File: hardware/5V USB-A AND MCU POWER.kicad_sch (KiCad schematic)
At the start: 34 parts, among them U19 NCP177BMX330TCG, U2 NCP177BMX330TCG, U3 NCP177BMX330TCG, U4 LMR14050-Q1, U5 NCP177AMX120TCG, U6 NCP177AMX120TCG

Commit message: messing arround with pcb to finalise
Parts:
- added TP12: TestPoint, TestPoint:TestPoint_Pad_D1.5mm, symbol Connector:TestPoint
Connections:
- net +5V: now also TP12.1
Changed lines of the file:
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@@
   (junction (at 67.31 124.46) (diameter 0) (color 0 0 0 0)
   )
+  (junction (at 151.13 68.58) (diameter 0) (color 0 0 0 0)
+  )
   (junction (at 33.02 160.02) (diameter 0) (color 0 0 0 0)
   )
@@
     (stroke (width 0) (type default))
   )
+  (wire (pts (xy 151.13 68.58) (xy 153.67 68.58))
+    (stroke (width 0) (type default))
+  )
   (wire (pts (xy 144.78 124.46) (xy 149.86 124.46))
     (stroke (width 0) (type default))
@@
     (stroke (width 0) (type default))
   )
-  (wire (pts (xy 148.59 68.58) (xy 153.67 68.58))
+  (wire (pts (xy 148.59 68.58) (xy 151.13 68.58))
     (stroke (width 0) (type default))
   )
@@
         )
       )
+    )
+  )
+  (symbol (lib_id "Connector:TestPoint") (at 151.13 68.58 0) (unit 1)
+    (in_bom yes) (on_board yes) (dnp no) (fields_autoplaced)
+    (property "Reference" "TP12" (at 152.527 64.6343 0)
+      (effects (font (size 1.27 1.27)) (justify left))
+    )
+    (property "Value" "TestPoint" (at 152.527 66.5553 0)
+      (effects (font (size 1.27 1.27)) (justify left))
+    )
+    (property "Footprint" "TestPoint:TestPoint_Pad_D1.5mm" (at 156.21 68.58 0)
+      (effects (font (size 1.27 1.27)) hide)
+    )
+    (property "Datasheet" "~" (at 156.21 68.58 0)
+      (effects (font (size 1.27 1.27)) hide)
+    )
+    (pin "1")
+    (instances
+      (project "usbc-car-module"
+        (path "/fae025e9-99c5-40c1-af6f-99dc1edbfa43/babd34fb-a18a-4bce-9735-4ab8ec7cd7ca"
+          (reference "TP12") (unit 1)
+        )
+      )

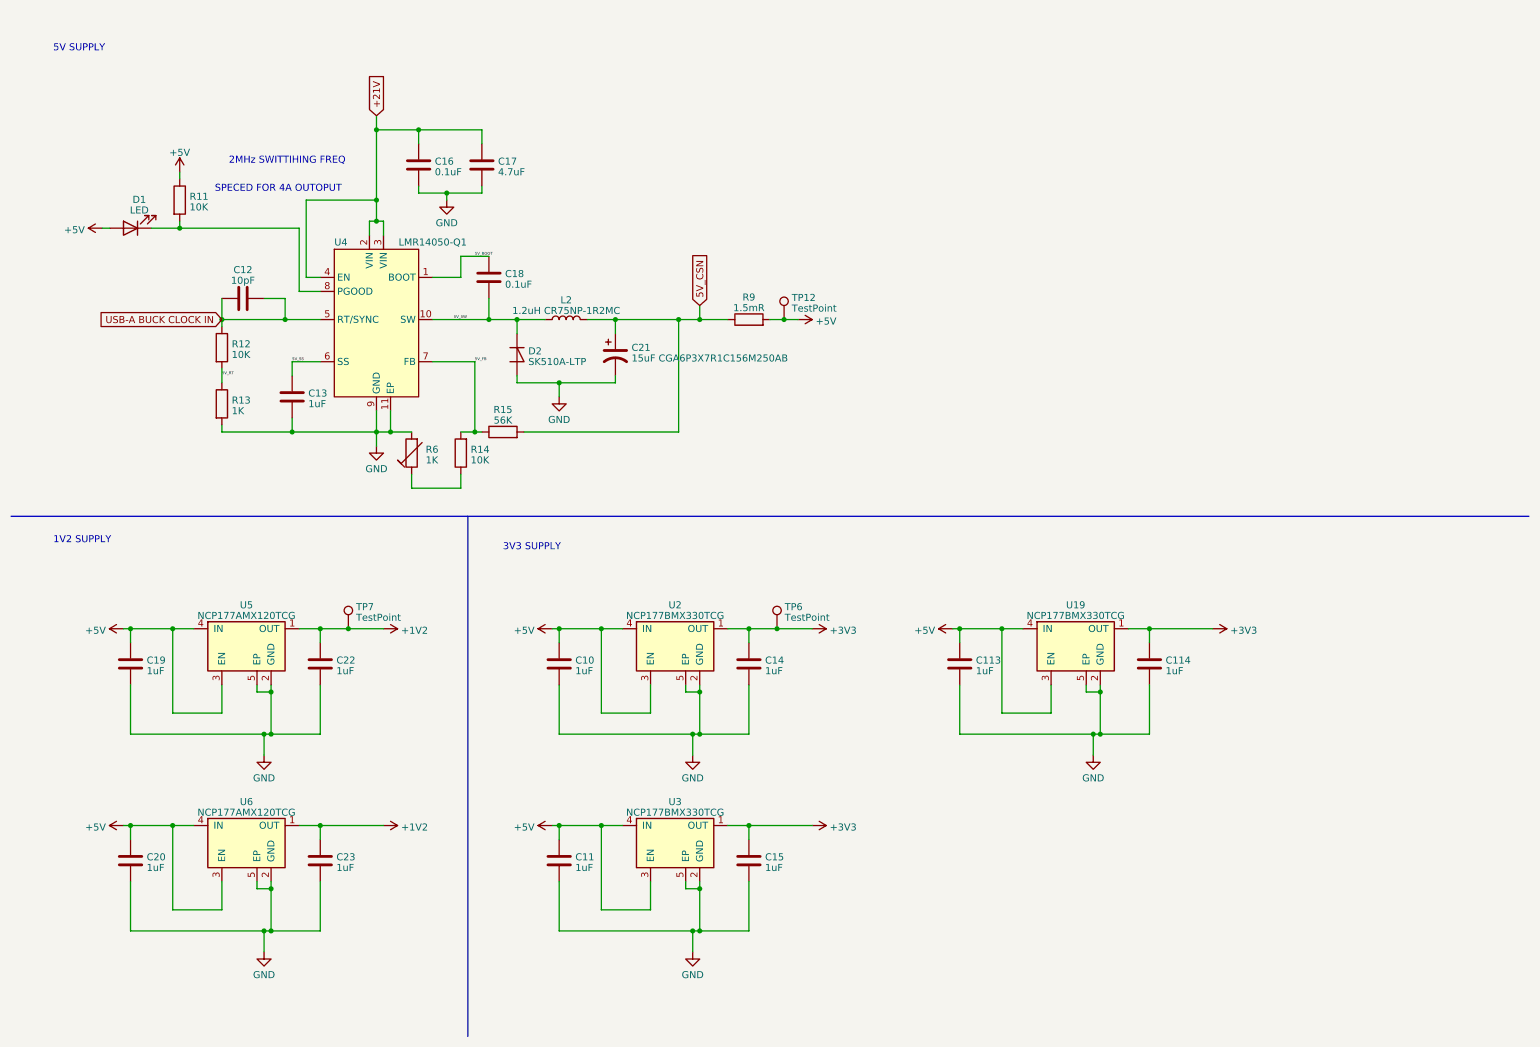
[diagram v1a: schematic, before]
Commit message: fixed DP issues and finneshed overall routeing
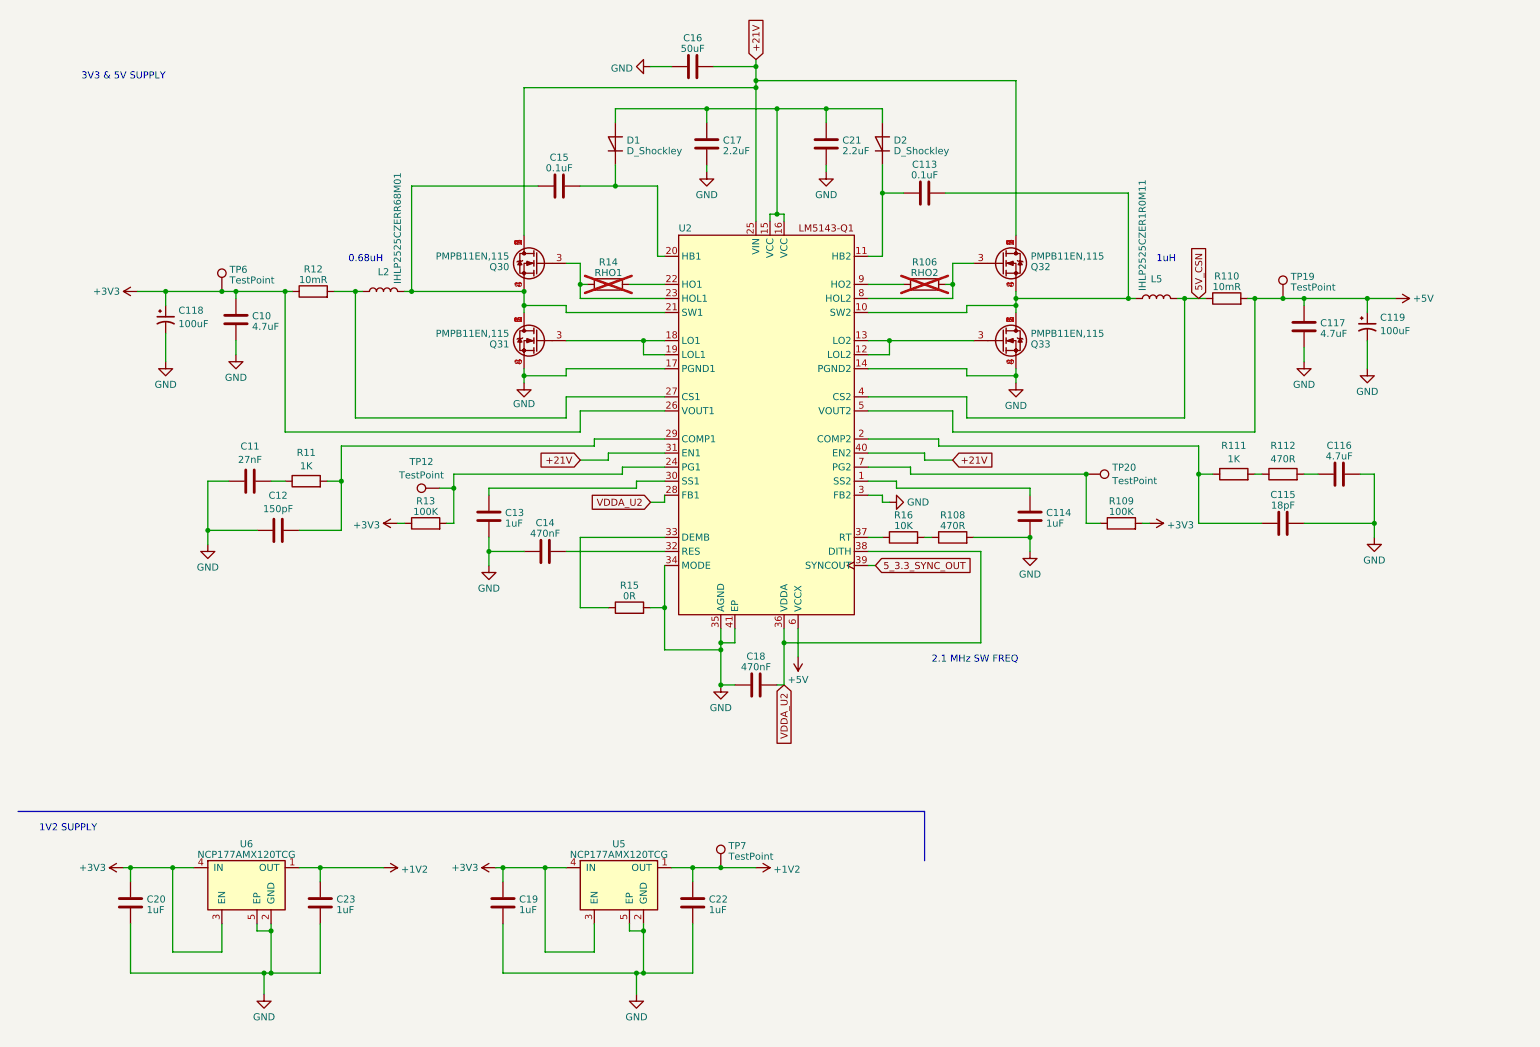
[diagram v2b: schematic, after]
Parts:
- removed C21: 15uF CGA6P3X7R1C156M250AB, Capacitor_SMD:C_1210_3225Metric, symbol Device:C_Polarized_US
- removed D1: LED, Diode_SMD:D_0603_1608Metric, symbol Device:LED
- removed R6: 1K, PCM_Potentiometer_SMD_AKL:Potentiometer_Bourns_TC33X_Vertical, symbol Device:R_Trim
- removed R9: 1.5mR, Resistor_SMD:R_2512_6332Metric, symbol Device:R
- removed U19, U2, U3: NCP177BMX330TCG, CARTHING:VREG_NCP170AMX300TCG, symbol CARTHING:NCP177BMX330TCG-Regulator_Linear
- removed U4: LMR14050-Q1, CARTHING:LMR14050, symbol EXTRA:LMR14050-Q1
- added C115: 18pF, Capacitor_SMD:C_0603_1608Metric, symbol Device:C
- added C116, C117: 4.7uF, Capacitor_SMD:C_0603_1608Metric, symbol Device:C
- added C118, C119: 100uF, Capacitor_SMD:CP_Elec_6.3x7.7, symbol Device:C_Polarized_Small_US
- added C21: 2.2uF, Capacitor_SMD:C_0603_1608Metric, symbol Device:C
- added D1: D_Shockley, Diode_SMD:D_SMA, symbol Device:D_Shockley
- added L5: IHLP2525CZER1R0M11, CARTHING:IND25X25CZ, symbol Device:L
- added Q30, Q31, Q32, Q33: PMPB11EN,115, CARTHING:TRANS_PMPB11EN_115, symbol Device:Q_NMOS_GDS
- added R106: RHO2, Resistor_SMD:R_0603_1608Metric, symbol Device:R
- added R108, R112: 470R, Resistor_SMD:R_0603_1608Metric, symbol Device:R
- added R109: 100K, Resistor_SMD:R_0603_1608Metric, symbol Device:R
- added R110: 10mR, Resistor_SMD:R_1206_3216Metric, symbol Device:R
- added R111: 1K, Resistor_SMD:R_0603_1608Metric, symbol Device:R
- added R16: 10K, Resistor_SMD:R_0603_1608Metric, symbol Device:R
- added TP19: TestPoint, TestPoint:TestPoint_Pad_D1.5mm, symbol Connector:TestPoint
- added TP20: TestPoint, TestPoint:TestPoint_Pad_D1.0mm, symbol Connector:TestPoint
- added U2: ~, CARTHING:LM5143, symbol CARTHING:LM5143-Q1
- C10: value 1uF -> 4.7uF
- C11: value 1uF -> 27nF
- C113, C15: value 1uF -> 0.1uF
- C12: value 10pF -> 150pF
- C14: value 1uF -> 470nF; footprint Capacitor_SMD:C_0603_1608Metric -> Capacitor_SMD:C_0805_2012Metric
- C16: value 0.1uF -> 50uF
- C17: value 4.7uF -> 2.2uF
- C18: value 0.1uF -> 470nF; footprint Capacitor_SMD:C_0603_1608Metric -> Capacitor_SMD:C_0805_2012Metric
- D2: value SK510A-LTP -> D_Shockley
- L2: value 1.2uH CR75NP-1R2MC -> IHLP2525CZERR68M01
- R11: value 10K -> 1K
- R12: value 10K -> 10mR; footprint Resistor_SMD:R_0603_1608Metric -> Resistor_SMD:R_1206_3216Metric
- R13: value 1K -> 100K
- R14: value 10K -> RHO1; now not fitted
- R15: value 56K -> 0R
- TP12: footprint TestPoint:TestPoint_Pad_D1.5mm -> TestPoint:TestPoint_Pad_D1.0mm
- TP6: footprint TestPoint:TestPoint_Pad_D1.0mm -> TestPoint:TestPoint_Pad_D1.5mm
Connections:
- net 5V_BOOT is gone; now on net GND: C18.1
- net 5V_SS is gone; now on net GND: C13.1
- net +21V: now also C16.2, Q30.1 (D), Q30.2 (D), Q30.5 (D), Q30.6 (D), Q30.7 (D), Q32.1 (D), Q32.2 (D), Q32.5 (D), Q32.6 (D), Q32.7 (D), U2.25 (VIN), U2.31 (EN1), U2.40 (EN2); no longer C16.1, C17.1
- net +3V3: now also C10.1, C19.1, C20.1, R12.1, R13.1, U5.3 (EN), U5.4 (IN), U6.3 (EN), U6.4 (IN), C118.1, R109.2, U2.26 (VOUT1); no longer C114.1, C14.1, C15.1
- net +5V: now also C117.1, C119.1, R110.2, TP19.1, U2.5 (VOUT2), U2.6 (VCCX); no longer C10.1, C11.1, C113.1, C19.1, C20.1, R11.1, TP12.1, U5.3 (EN), U5.4 (IN), U6.3 (EN), U6.4 (IN)
- net 5V_CSN: now also L5.2, R110.1, U2.4 (CS2); no longer L2.2, R15.2
- net GND: now also C11.1, C114.1, C12.1, C14.1, C16.1, R15.2, C115.2, C116.2, C117.2, C118.2, C119.2, C21.2, Q31.4 (S), Q31.8 (S), Q33.4 (S), Q33.8 (S), R108.2, U2.14 (PGND2), U2.17 (PGND1), U2.3 (FB2), U2.34 (MODE), U2.35 (AGND), U2.41 (EP); no longer C11.2, C113.2, C114.2, C13.2, C14.2, C15.2, C16.2, D2.2 (A), R13.2
- net at R11.2: now also C12.2, U2.29 (COMP1)
- net at R14.1: now also Q30.3 (G), U2.23 (HOL1)
- net 5V_FB: no longer names the net of R14.2
- net 5V_FB: now also U2.22 (HO1); no longer R15.1
- net 5V_RT: no longer names the net of R12.2
- net 5V_RT: now also L2.1, U2.27 (CS1); no longer R13.1
- removed net 5V_SW: C18.2, D2.1 (K), L2.1
- removed net USB-A BUCK CLOCK IN: C12.1, C12.2, R12.1
- new net: C114.2, U2.1 (SS2)
- new net: C113.2, L5.1, Q32.4 (S), Q32.8 (S), Q33.1 (D), Q33.2 (D), Q33.5 (D), Q33.6 (D), Q33.7 (D), U2.10 (SW2)
- new net: C113.1, D2.1 (K), U2.11 (HB2)
- new net: Q33.3 (G), U2.12 (LOL2), U2.13 (LO2)
- new net: C17.1, C21.1, D1.2 (A), D2.2 (A), U2.15 (VCC), U2.16 (VCC)
- new net: Q31.3 (G), U2.18 (LO1), U2.19 (LOL1)
- new net: C115.1, R111.1, U2.2 (COMP2)
- new net: C15.2, D1.1 (K), U2.20 (HB1)
- new net: C15.1, L2.2, Q30.4 (S), Q30.8 (S), Q31.1 (D), Q31.2 (D), Q31.5 (D), Q31.6 (D), Q31.7 (D), U2.21 (SW1)
- new net: R13.2, TP12.1, U2.24 (PG1)
- new net: C13.2, U2.30 (SS1)
- new net: C14.2, U2.32 (RES)
- new net: R15.1, U2.33 (DEMB)
- new net: R16.1, U2.37 (RT)
- new net: R109.1, TP20.1, U2.7 (PG2)
- new net: Q32.3 (G), R106.2, U2.8 (HOL2)
- new net: R106.1, U2.9 (HO2)
- new net: C11.2, R11.1
- new net: R108.1, R16.2
- new net: R111.2, R112.1
- new net: C116.1, R112.2
- new net 5_3.3_SYNC_OUT: U2.39 (SYNCOUT)
- new net VDDA_U2: C18.2, U2.28 (FB1), U2.36 (VDDA), U2.38 (DITH)
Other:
- note added: "0.68uH"
- note added: "1uH"
- note added: "2.1 MHz SW FREQ"
- note added: "3V3 & 5V SUPPLY"
- note removed: "2MHz SWITTIHING FREQ"
- note removed: "3V3 SUPPLY"
- note removed: "5V SUPPLY"
- note removed: "SPECED FOR 4A OUTOPUT"
- moved on the sheet: C19, C20, C22, C23, TP7, U5, U6

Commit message: minor revisions
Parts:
- D1, D2: footprint Diode_SMD:D_SMA -> Diode_SMD:D_SOD-523
- U2: value ~ -> LM5143
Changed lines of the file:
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@@
       (effects (font (size 1.27 1.27)) (justify left))
     )
-    (property "Value" "~" (at 157.48 67.31 0)
+    (property "Value" "LM5143" (at 157.48 67.31 0)
       (effects (font (size 1.27 1.27)))
     )
@@
       (effects (font (size 1.27 1.27)) (justify right))
     )
-    (property "Footprint" "Diode_SMD:D_SMA" (at 120.65 36.83 0)
+    (property "Footprint" "Diode_SMD:D_SOD-523" (at 120.65 36.83 0)
       (effects (font (size 1.27 1.27)) hide)
     )
@@
       (effects (font (size 1.27 1.27)) (justify right))
     )
-    (property "Footprint" "Diode_SMD:D_SMA" (at 168.91 36.83 0)
-      (effects (font (size 1.27 1.27)) hide)
-    )
+    (property "Footprint" "Diode_SMD:D_SOD-523" (at 168.91 36.83 0)
+      (effects (font (size 1.27 1.27)) hide)
+    )

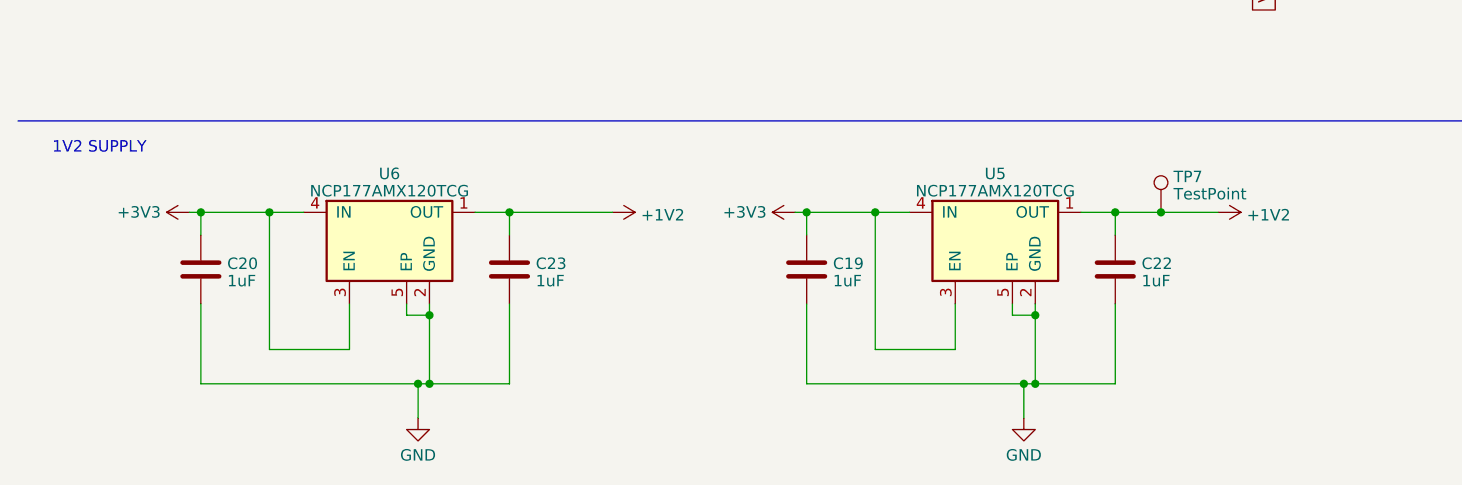
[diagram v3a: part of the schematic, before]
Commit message: updated block digram minor pcb changes
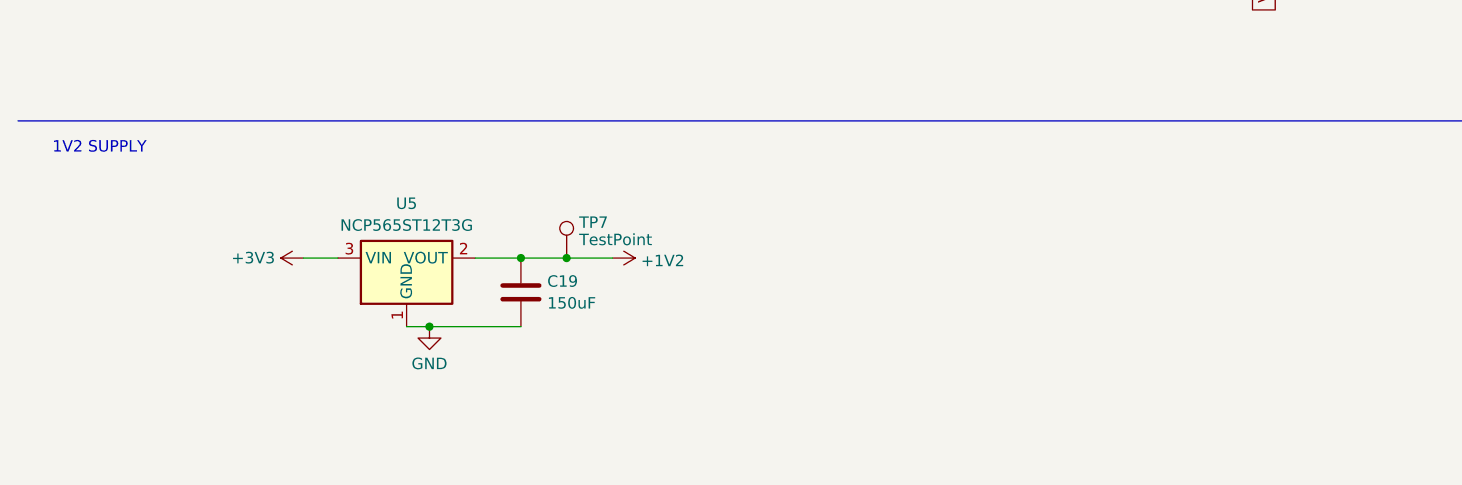
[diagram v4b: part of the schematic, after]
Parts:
- removed C20, C22, C23: 1uF, Capacitor_SMD:C_0603_1608Metric, symbol Device:C
- removed U5, U6: NCP177AMX120TCG, CARTHING:VREG_NCP170AMX300TCG, symbol CARTHING:NCP177BMX330TCG-Regulator_Linear
- added U5: NCP565ST12T3G, Package_TO_SOT_SMD:SOT-223-3_TabPin2, symbol Regulator_Linear:AMS1117
- C19: value 1uF -> 150uF; footprint Capacitor_SMD:C_0603_1608Metric -> Capacitor_SMD:C_1206_3216Metric
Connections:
- net +1V2: now also C19.1, U5.2 (VOUT)
- net +3V3: now also U5.3 (VIN); no longer C19.1
- net GND: now also U5.1 (GND)
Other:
- moved on the sheet: TP7

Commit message: switched can tranceiver to combo controler and tranceiver
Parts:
- TP6: footprint TestPoint:TestPoint_Pad_D1.5mm -> TestPoint:TestPoint_Pad_D1.0mm
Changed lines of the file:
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@@
 			)
 		)
-		(property "Footprint" "TestPoint:TestPoint_Pad_D1.5mm"
+		(property "Footprint" "TestPoint:TestPoint_Pad_D1.0mm"
 			(at 54.61 63.5 0)
 			(effects
